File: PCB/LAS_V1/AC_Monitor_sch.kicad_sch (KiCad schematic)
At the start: 12 parts, among them U4 LM393

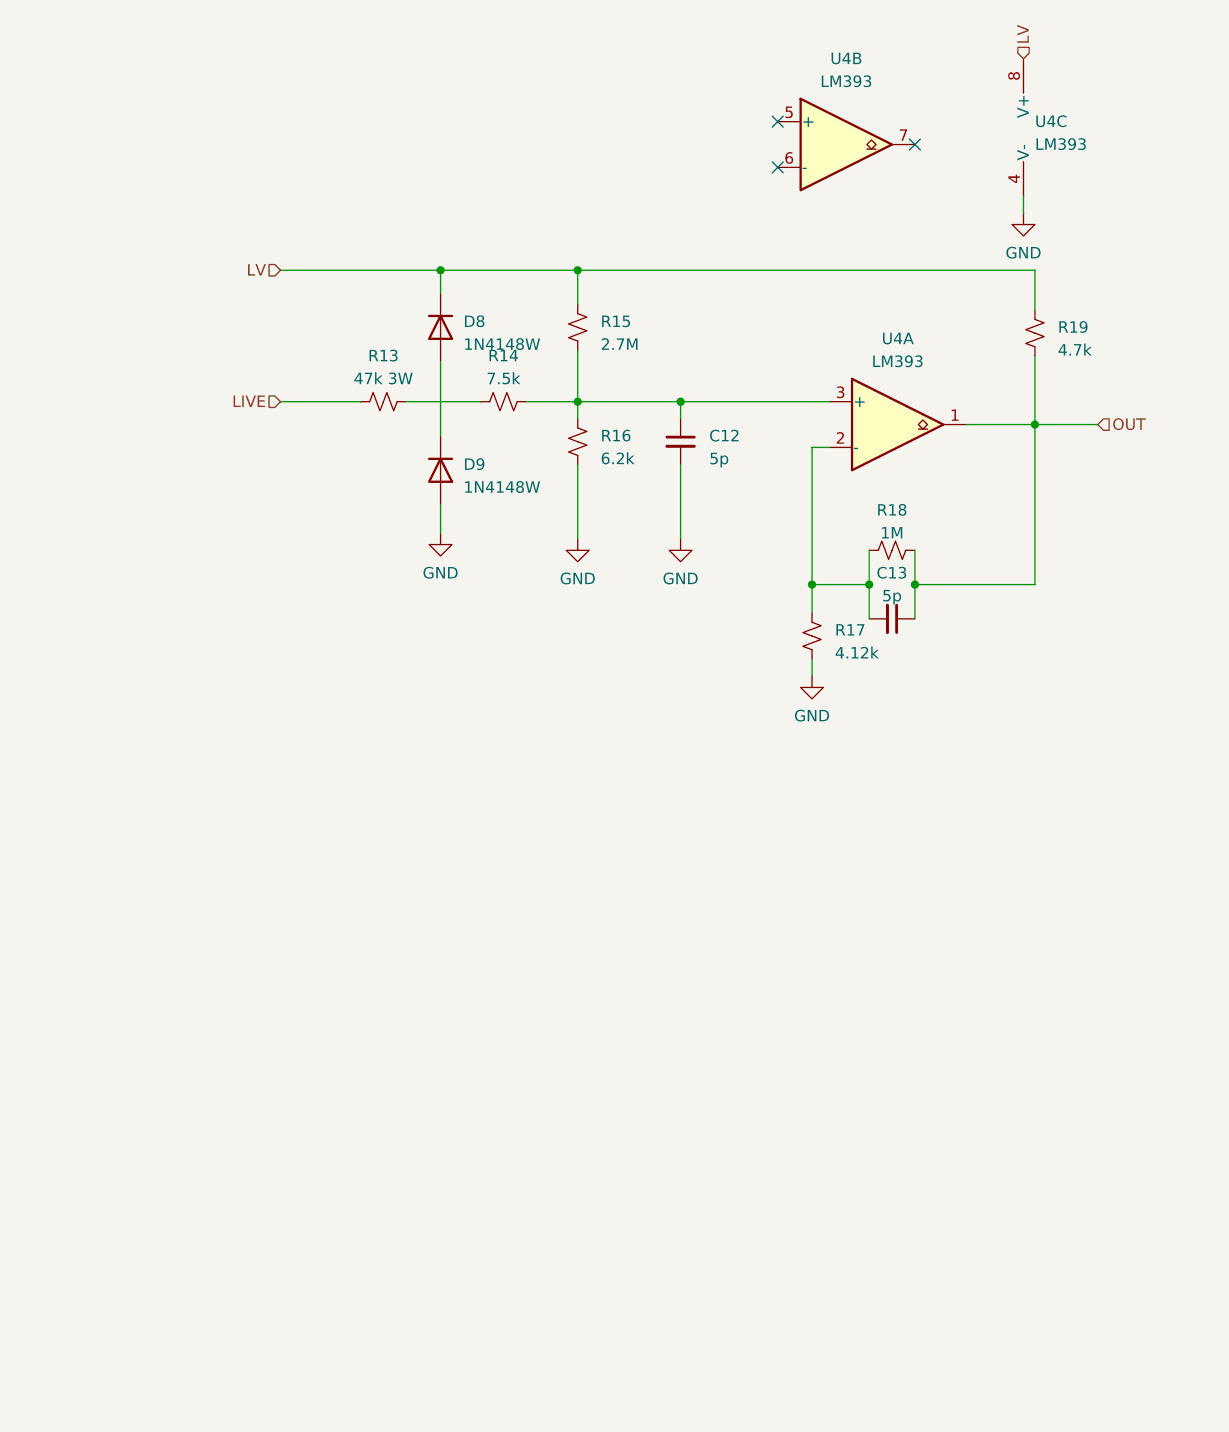
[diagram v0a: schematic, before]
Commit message: added JLBPCB part Numbers
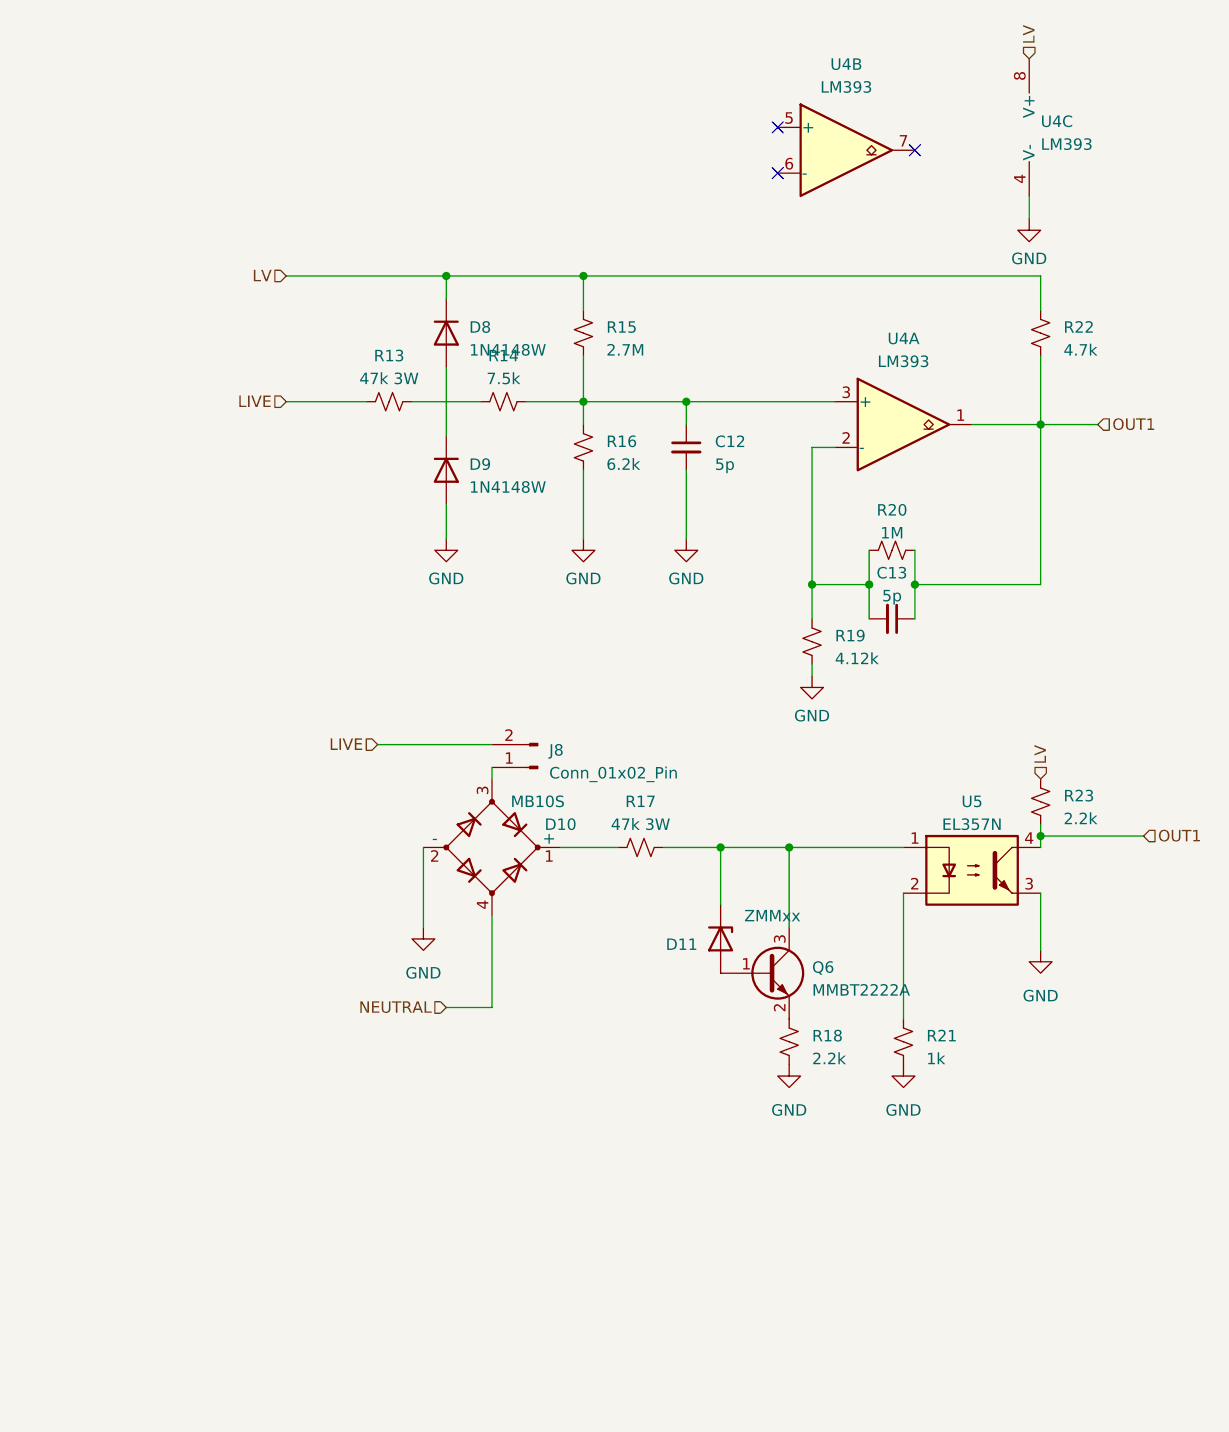
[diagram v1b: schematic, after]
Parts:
- added D10: MB10S, Custom:MBS_L4.7-W3.8-P2.40-LS7.0-TL, symbol Device:D_Bridge_+-AA
- added D11: ZMMxx, Diode_SMD:D_MiniMELF, symbol Diode:ZMMxx
- added J8: Conn_01x02_Pin, Connector_PinHeader_1.27mm:PinHeader_1x02_P1.27mm_Vertical, symbol Connector:Conn_01x02_Pin
- added Q6: MMBT2222A, Package_TO_SOT_SMD:SOT-23, symbol Transistor_BJT:MMBT3904
- added R17: 47k 3W, Resistor_THT:R_Axial_DIN0617_L17.0mm_D6.0mm_P25.40mm_Horizontal, symbol Device:R_Small_US
- added R18, R23: 2.2k, symbol Device:R_Small_US
- added R21: 1k, Resistor_SMD:R_0603_1608Metric, symbol Device:R_Small_US
- added U5: EL357N, Package_SO:SOP-4_3.8x4.1mm_P2.54mm, symbol Isolator:LTV-817M
- R13: footprint (none) -> Resistor_THT:R_Axial_DIN0617_L17.0mm_D6.0mm_P25.40mm_Horizontal; LCSC (none) -> C714661
- renumbered R17 to R19, R18 to R20, R19 to R22
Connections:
- net GND: now also D10.2 (-), R18.1, R21.1, U5.3
- net LIVE: now also J8.2 (Pin_2)
- net LV: now also R23.2
- net OUT renamed OUT1
- net OUT1: now also R23.1, U5.4
- new net: D10.1 (+), R17.1
- new net: D10.3, J8.1 (Pin_1)
- new net: D11.1 (K), Q6.3 (C), R17.2, U5.1
- new net: R21.2, U5.2
- new net: D11.2 (A), Q6.1 (B)
- new net: Q6.2 (E), R18.2
- new net NEUTRAL: D10.4
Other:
- moved on the sheet: C12, D8, D9, R13, R15, R16, R19, R22, U4A, U4B, U4C

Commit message: All components Placed on PCB
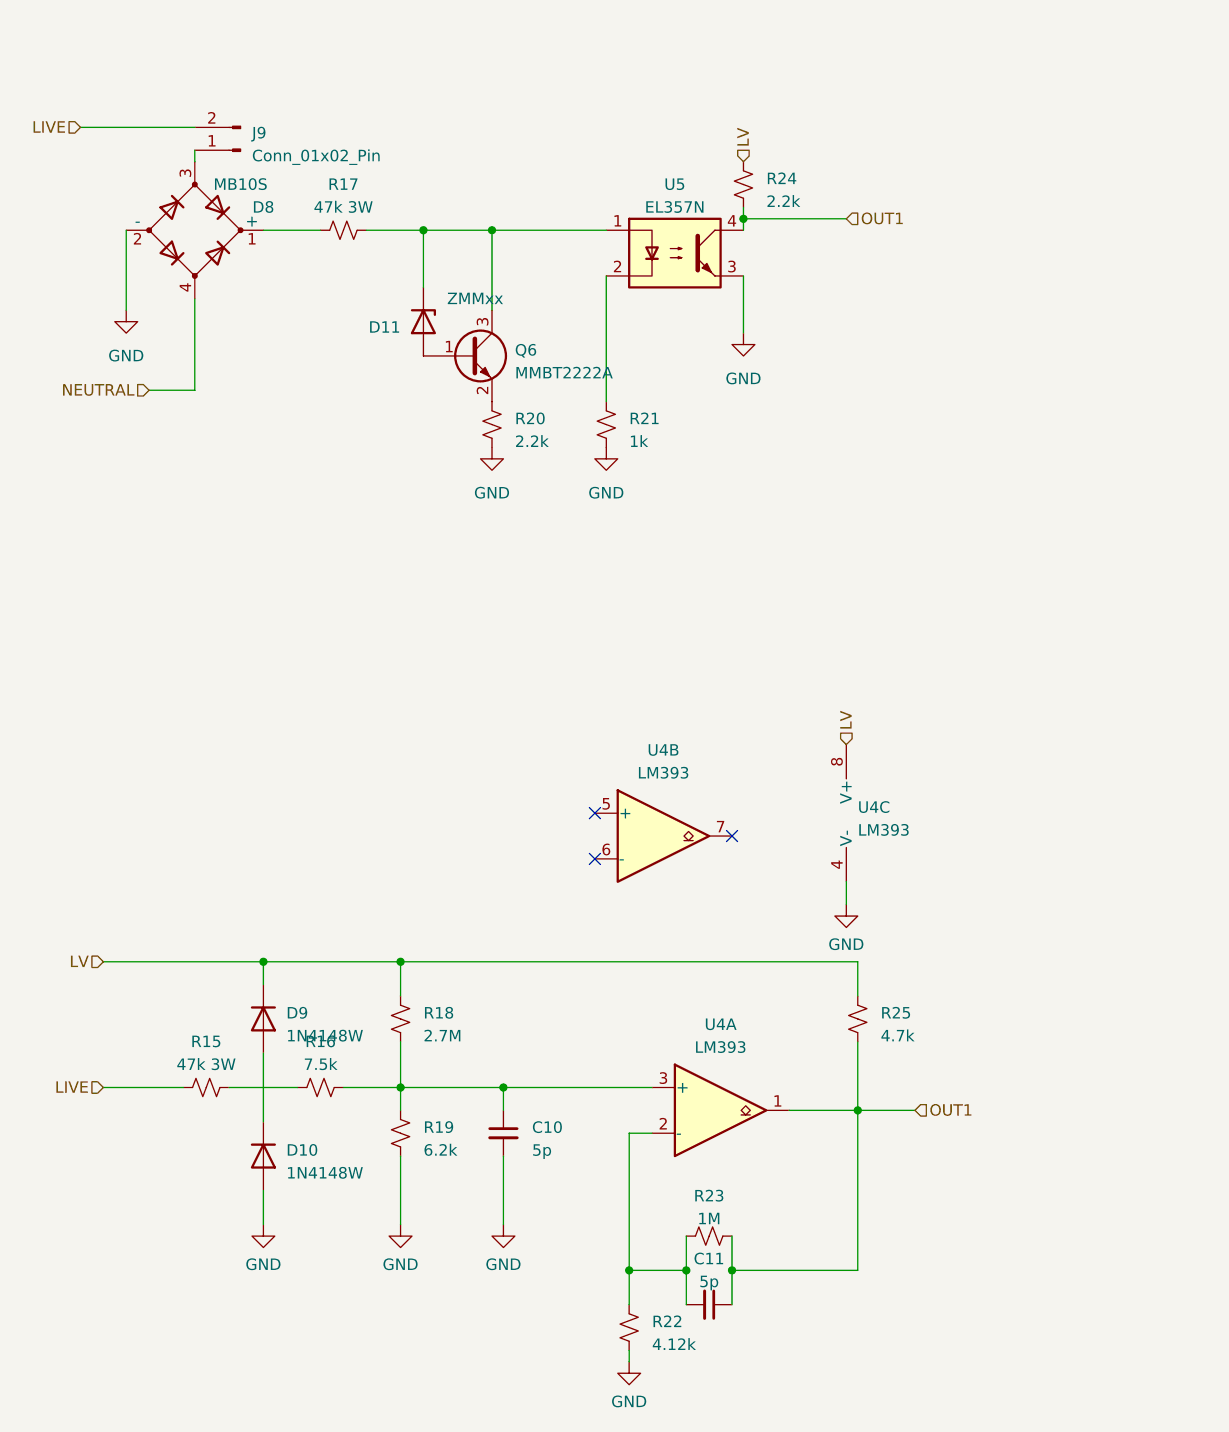
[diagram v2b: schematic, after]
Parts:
- removed C12, C13: 5p, symbol Device:C_Small
- removed D8: 1N4148W, Diode_SMD:D_SOD-123, symbol Diode:1N4148W
- removed R13: 47k 3W, Resistor_THT:R_Axial_DIN0617_L17.0mm_D6.0mm_P25.40mm_Horizontal, symbol Device:R_Small_US
- removed R14: 7.5k, symbol Device:R_Small_US
- removed R20: 1M, symbol Device:R_Small_US
- added C10, C11: 5p, symbol Device:C_Small
- added D10: 1N4148W, Diode_SMD:D_SOD-123, symbol Diode:1N4148W
- added R18: 2.7M, symbol Device:R_Small_US
- added R23: 1M, symbol Device:R_Small_US
- added R25: 4.7k, symbol Device:R_Small_US
- R15: value 2.7M -> 47k 3W; footprint (none) -> Resistor_THT:R_Axial_DIN0617_L17.0mm_D6.0mm_P25.40mm_Horizontal; LCSC (none) -> C714661
- R16: value 6.2k -> 7.5k
- R19: value 4.12k -> 6.2k
- R20: renamed from R18; footprint (none) -> Resistor_SMD:R_0603_1608Metric; LCSC C714661 -> C4190
- R22: value 4.7k -> 4.12k
- R24: renamed from R23; footprint (none) -> Resistor_SMD:R_0603_1608Metric; LCSC C714661 -> C4190
- U5: LCSC (none) -> C29981
- renumbered D10 to D8, J8 to J9
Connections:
- net GND: now also R22.1, C10.2, D10.2 (A); no longer D9.2 (A), R16.1
- net LIVE: now also R15.1
- net LV: now also D9.1 (K), R18.2, R25.2; no longer R15.2, R22.2
- net OUT1: now also C11.1, R23.1, R25.1; no longer R22.1
- net at R16.2, U4.3 (+): now also R19.2, C10.1, R18.1; no longer R15.1
- net at U4.2 (-): now also R22.2, C11.2, R23.2; no longer R19.2
- new net: D10.1 (K), D9.2 (A)
- new net: R15.2, R16.1
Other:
- moved on the sheet: D11, D8, J9, Q6, R17, R20, R21, R24, U5

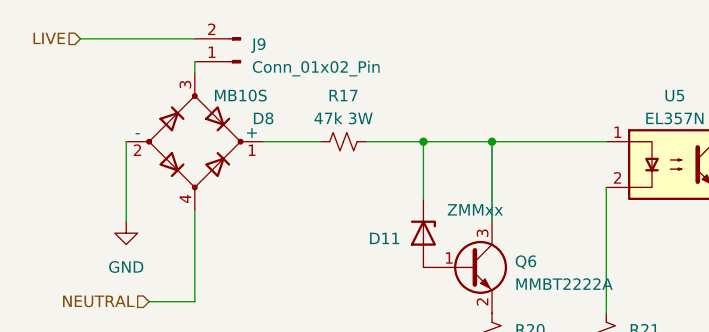
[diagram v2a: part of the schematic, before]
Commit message: PCB V1 complete
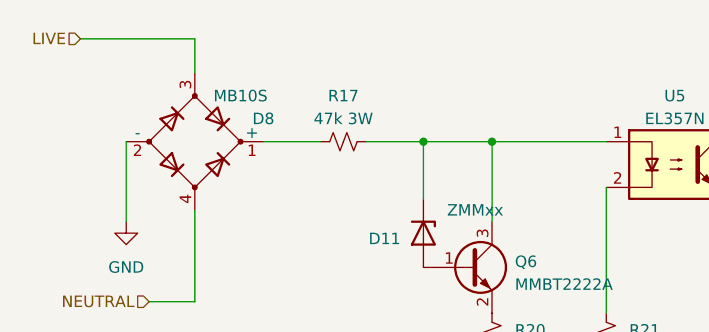
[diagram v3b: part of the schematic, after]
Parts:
- removed J9: Conn_01x02_Pin, Connector_PinHeader_1.27mm:PinHeader_1x02_P1.27mm_Vertical, symbol Connector:Conn_01x02_Pin
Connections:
- net LIVE: now also D8.3
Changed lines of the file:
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@@
     (stroke (width 0) (type default))
   )
-  (wire (pts (xy 57.15 30.48) (xy 57.15 31.75))
+  (wire (pts (xy 57.15 27.94) (xy 57.15 31.75))
     (stroke (width 0) (type default))
   )
@@
         )
       )
-    )
-  )
-  (symbol (lib_id "Connector:Conn_01x02_Pin") (at 62.23 30.48 180) (unit 1)
-    (in_bom yes) (on_board yes) (dnp no) (fields_autoplaced)
-    (property "Reference" "J9" (at 63.5 28.575 0)
-      (effects (font (size 1.27 1.27)) (justify right))
-    )
-    (property "Value" "Conn_01x02_Pin" (at 63.5 31.115 0)
-      (effects (font (size 1.27 1.27)) (justify right))
-    )
-    (property "Footprint" "Connector_PinHeader_1.27mm:PinHeader_1x02_P1.27mm_Vertical" (at 62.23 30.48 0)
-      (effects (font (size 1.27 1.27)) hide)
-    )
-    (property "Datasheet" "~" (at 62.23 30.48 0)
-      (effects (font (size 1.27 1.27)) hide)
-    )
-    (pin "1")
-    (pin "2")
-    (instances
-      (project "LAS_V1"
-        (path "/aadef4b8-3115-4a49-998f-828f2021a6b4/e3f941ed-5575-4c88-95e0-e32be2fe0df6"
-          (reference "J9") (unit 1)
-        )
-      )
